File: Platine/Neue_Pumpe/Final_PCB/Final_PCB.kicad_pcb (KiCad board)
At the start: 2 copper layers, 27.5 x 27.5 mm, 1 part

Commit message: a lot of advance in final PCB
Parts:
- added C1: 100p, Capacitor_SMD:C_0603_1608Metric_Pad1.08x0.95mm_HandSolder, F.Cu at (50.1, -51.1)
- added C10: 100p, Capacitor_SMD:C_0603_1608Metric_Pad1.08x0.95mm_HandSolder, F.Cu at (50.1, -28.5)
- added C11: 100p, Capacitor_SMD:C_0603_1608Metric_Pad1.08x0.95mm_HandSolder, F.Cu at (50.1, -26.0)
- added C12: 100p, Capacitor_SMD:C_0603_1608Metric_Pad1.08x0.95mm_HandSolder, F.Cu at (50.1, -23.5)
- added C13: 100p, Capacitor_SMD:C_0603_1608Metric_Pad1.08x0.95mm_HandSolder, F.Cu at (50.1, -21.0)
- added C14: 100p, Capacitor_SMD:C_0603_1608Metric_Pad1.08x0.95mm_HandSolder, F.Cu at (54.5, -51.1)
- added C15: 100p, Capacitor_SMD:C_0603_1608Metric_Pad1.08x0.95mm_HandSolder, F.Cu at (54.5, -48.6)
- added C16: 100p, Capacitor_SMD:C_0603_1608Metric_Pad1.08x0.95mm_HandSolder, F.Cu at (54.5, -46.1)
- added C17: 100p, Capacitor_SMD:C_0603_1608Metric_Pad1.08x0.95mm_HandSolder, F.Cu at (54.5, -43.6)
- added C18: 100p, Capacitor_SMD:C_0603_1608Metric_Pad1.08x0.95mm_HandSolder, F.Cu at (54.5, -41.1)
- added C19: 100n, Capacitor_SMD:C_0603_1608Metric_Pad1.08x0.95mm_HandSolder, F.Cu at (54.5, -38.6)
- added C2: 100p, Capacitor_SMD:C_0603_1608Metric_Pad1.08x0.95mm_HandSolder, F.Cu at (50.1, -48.6)
- added C20: 100n, Capacitor_SMD:C_0603_1608Metric_Pad1.08x0.95mm_HandSolder, F.Cu at (54.5, -36.1)
- added C21: 100n, Capacitor_SMD:C_0603_1608Metric_Pad1.08x0.95mm_HandSolder, F.Cu at (54.5, -33.5)
- added C22: 10u, Capacitor_SMD:C_0603_1608Metric_Pad1.08x0.95mm_HandSolder, F.Cu at (78.2, 6.53)
- added C23: 10u, Capacitor_SMD:C_0603_1608Metric_Pad1.08x0.95mm_HandSolder, F.Cu at (78.2, 9.04)
- added C24: 0.1uF, Capacitor_SMD:C_0603_1608Metric_Pad1.08x0.95mm_HandSolder, F.Cu at (79.1, 37.1)
- added C25: 0.1uF, Capacitor_SMD:C_0603_1608Metric_Pad1.08x0.95mm_HandSolder, F.Cu at (79.3, 28.1)
- added C26: 0.1uF, Capacitor_SMD:C_0603_1608Metric_Pad1.08x0.95mm_HandSolder, F.Cu at (93.5, 41.6)
- added C27: 0.1uF, Capacitor_SMD:C_0603_1608Metric_Pad1.08x0.95mm_HandSolder, F.Cu at (86.3, 37.5)
- added C28: 0.1uF, Capacitor_SMD:C_0603_1608Metric_Pad1.08x0.95mm_HandSolder, F.Cu at (72.4, 37.1)
- added C29: 0.1uF, Capacitor_SMD:C_0603_1608Metric_Pad1.08x0.95mm_HandSolder, F.Cu at (72.3, 28.1)
- added C3: 100p, Capacitor_SMD:C_0603_1608Metric_Pad1.08x0.95mm_HandSolder, F.Cu at (50.1, -46.1)
- added C30: 0.1uF, Capacitor_SMD:C_0603_1608Metric_Pad1.08x0.95mm_HandSolder, B.Cu at (80.3, 43.1)
- added C31: 0.1uF, Capacitor_SMD:C_0603_1608Metric_Pad1.08x0.95mm_HandSolder, F.Cu at (65.8, 37.1)
- added C32: 0.1uF, Capacitor_SMD:C_0603_1608Metric_Pad1.08x0.95mm_HandSolder, B.Cu at (78.3, 35.7)
- added C33: 0.1uF, Capacitor_SMD:C_0603_1608Metric_Pad1.08x0.95mm_HandSolder, F.Cu at (82.6, -26.4)
- added C34: 0.1uF, Capacitor_SMD:C_0603_1608Metric_Pad1.08x0.95mm_HandSolder, F.Cu at (82.6, -23.9)
- added C35: 0.1uF, Capacitor_SMD:C_0603_1608Metric_Pad1.08x0.95mm_HandSolder, F.Cu at (82.6, -21.3)
- added C36: 0.1uF, Capacitor_SMD:C_0603_1608Metric_Pad1.08x0.95mm_HandSolder, F.Cu at (82.6, -18.8)
- added C37: 0.1uF, Capacitor_SMD:C_0603_1608Metric_Pad1.08x0.95mm_HandSolder, F.Cu at (66.6, 28.1)
- added C38: 0.1uF, Capacitor_SMD:C_0603_1608Metric_Pad1.08x0.95mm_HandSolder, F.Cu at (86.9, -31.4)
- added C39: 0.1uF, Capacitor_SMD:C_0603_1608Metric_Pad1.08x0.95mm_HandSolder, F.Cu at (86.9, -28.9)
- added C4: 100p, Capacitor_SMD:C_0603_1608Metric_Pad1.08x0.95mm_HandSolder, F.Cu at (50.1, -43.6)
- added C40: 0.1uF, Capacitor_SMD:C_0603_1608Metric_Pad1.08x0.95mm_HandSolder, F.Cu at (86.9, -26.4)
- added C41: 0.1uF, Capacitor_SMD:C_0603_1608Metric_Pad1.08x0.95mm_HandSolder, F.Cu at (86.9, -23.9)
- added C5: 100p, Capacitor_SMD:C_0603_1608Metric_Pad1.08x0.95mm_HandSolder, F.Cu at (50.1, -41.1)
- added C6: 100p, Capacitor_SMD:C_0603_1608Metric_Pad1.08x0.95mm_HandSolder, F.Cu at (50.1, -38.6)
- added C7: 100p, Capacitor_SMD:C_0603_1608Metric_Pad1.08x0.95mm_HandSolder, F.Cu at (50.1, -36.1)
- added C8: 100p, Capacitor_SMD:C_0603_1608Metric_Pad1.08x0.95mm_HandSolder, F.Cu at (50.1, -33.5)
- added C9: 100p, Capacitor_SMD:C_0603_1608Metric_Pad1.08x0.95mm_HandSolder, F.Cu at (50.1, -31.0)
- added J3: Conn_01x10, FLE-105-01-G-DV-K-TR:FLE-105-01-X-DV-Y-TR, B.Cu at (38.8, 38.0)
- added J4: Conn_01x10, Samtec-FTSH-105-01-L-DV-K:FTSH-105-01-L-DV-K, F.Cu at (72.4, 41.7)
- added J5: Conn_01x10, FLE-105-01-G-DV-K-TR:FLE-105-01-X-DV-Y-TR, B.Cu at (39.3, 72.5)
- added J6: Conn_01x06, Connector_PinHeader_1.27mm:PinHeader_2x03_P1.27mm_Vertical_SMD, B.Cu at (77.8, 46.3)
- added J7: Conn_01x06, Connector_PinHeader_1.27mm:PinHeader_2x03_P1.27mm_Vertical_SMD, B.Cu at (73.1, 41.4)
- added R1: 1k, Resistor_SMD:R_0603_1608Metric_Pad0.98x0.95mm_HandSolder, F.Cu at (54.5, -31.0)
- added R10: 1k, Resistor_SMD:R_0603_1608Metric_Pad0.98x0.95mm_HandSolder, F.Cu at (58.8, -41.1)
- added R11: 100k, Resistor_SMD:R_0603_1608Metric_Pad0.98x0.95mm_HandSolder, F.Cu at (58.8, -38.6)
- added R12: 100k, Resistor_SMD:R_0603_1608Metric_Pad0.98x0.95mm_HandSolder, F.Cu at (58.8, -36.1)
- added R13: 100k, Resistor_SMD:R_0603_1608Metric_Pad0.98x0.95mm_HandSolder, F.Cu at (58.8, -33.5)
- added R14: 100k, Resistor_SMD:R_0603_1608Metric_Pad0.98x0.95mm_HandSolder, F.Cu at (58.8, -31.0)
- added R15: 252k, Resistor_SMD:R_0603_1608Metric_Pad0.98x0.95mm_HandSolder, F.Cu at (58.8, -28.5)
- added R16: 252k, Resistor_SMD:R_0603_1608Metric_Pad0.98x0.95mm_HandSolder, F.Cu at (58.8, -26.0)
- added R17: 252k, Resistor_SMD:R_0603_1608Metric_Pad0.98x0.95mm_HandSolder, F.Cu at (58.8, -23.5)
- added R18: 252k, Resistor_SMD:R_0603_1608Metric_Pad0.98x0.95mm_HandSolder, F.Cu at (58.8, -21.0)
- added R19: 1k, Resistor_SMD:R_0603_1608Metric_Pad0.98x0.95mm_HandSolder, F.Cu at (63.2, -51.1)
- added R2: 1k, Resistor_SMD:R_0603_1608Metric_Pad0.98x0.95mm_HandSolder, F.Cu at (54.5, -28.5)
- added R20: 1k, Resistor_SMD:R_0603_1608Metric_Pad0.98x0.95mm_HandSolder, F.Cu at (63.2, -48.6)
- added R21: 1k, Resistor_SMD:R_0603_1608Metric_Pad0.98x0.95mm_HandSolder, F.Cu at (63.2, -46.1)
- added R22: 1k, Resistor_SMD:R_0603_1608Metric_Pad0.98x0.95mm_HandSolder, F.Cu at (63.2, -43.6)
- added R23: 1k, Resistor_SMD:R_0603_1608Metric_Pad0.98x0.95mm_HandSolder, F.Cu at (63.2, -41.1)
- added R24: 1k, Resistor_SMD:R_0603_1608Metric_Pad0.98x0.95mm_HandSolder, F.Cu at (63.2, -38.6)
- added R25: 100k, Resistor_SMD:R_0603_1608Metric_Pad0.98x0.95mm_HandSolder, F.Cu at (63.2, -36.1)
- added R26: 100k, Resistor_SMD:R_0603_1608Metric_Pad0.98x0.95mm_HandSolder, F.Cu at (63.2, -33.5)
- added R27: 100k, Resistor_SMD:R_0603_1608Metric_Pad0.98x0.95mm_HandSolder, F.Cu at (63.2, -31.0)
- added R28: 100k, Resistor_SMD:R_0603_1608Metric_Pad0.98x0.95mm_HandSolder, F.Cu at (63.2, -28.5)
- added R29: 100k, Resistor_SMD:R_0603_1608Metric_Pad0.98x0.95mm_HandSolder, F.Cu at (63.2, -26.0)
- added R3: 100k, Resistor_SMD:R_0603_1608Metric_Pad0.98x0.95mm_HandSolder, F.Cu at (54.5, -26.0)
- added R30: 100k, Resistor_SMD:R_0603_1608Metric_Pad0.98x0.95mm_HandSolder, F.Cu at (63.2, -23.5)
- added R31: 252k, Resistor_SMD:R_0603_1608Metric_Pad0.98x0.95mm_HandSolder, F.Cu at (63.2, -21.0)
- added R32: 252k, Resistor_SMD:R_0603_1608Metric_Pad0.98x0.95mm_HandSolder, F.Cu at (67.5, -51.1)
- added R33: 252k, Resistor_SMD:R_0603_1608Metric_Pad0.98x0.95mm_HandSolder, F.Cu at (67.5, -48.6)
- added R34: 252k, Resistor_SMD:R_0603_1608Metric_Pad0.98x0.95mm_HandSolder, F.Cu at (67.5, -46.1)
- added R35: 252k, Resistor_SMD:R_0603_1608Metric_Pad0.98x0.95mm_HandSolder, F.Cu at (67.5, -43.6)
- added R36: 252k, Resistor_SMD:R_0603_1608Metric_Pad0.98x0.95mm_HandSolder, F.Cu at (67.5, -41.1)
- added R37: 1k, Resistor_SMD:R_0603_1608Metric_Pad0.98x0.95mm_HandSolder, F.Cu at (67.5, -38.6)
- added R38: 1k, Resistor_SMD:R_0603_1608Metric_Pad0.98x0.95mm_HandSolder, F.Cu at (67.5, -36.1)
- added R39: 1k, Resistor_SMD:R_0603_1608Metric_Pad0.98x0.95mm_HandSolder, F.Cu at (67.5, -33.5)
- added R4: 100k, Resistor_SMD:R_0603_1608Metric_Pad0.98x0.95mm_HandSolder, F.Cu at (54.5, -23.5)
- added R40: 1k, Resistor_SMD:R_0603_1608Metric_Pad0.98x0.95mm_HandSolder, F.Cu at (67.5, -31.0)
- added R41: 1k, Resistor_SMD:R_0603_1608Metric_Pad0.98x0.95mm_HandSolder, F.Cu at (67.5, -28.5)
- added R42: 1k, Resistor_SMD:R_0603_1608Metric_Pad0.98x0.95mm_HandSolder, F.Cu at (67.5, -26.0)
- added R43: 100k, Resistor_SMD:R_0603_1608Metric_Pad0.98x0.95mm_HandSolder, F.Cu at (67.5, -23.5)
- added R44: 100k, Resistor_SMD:R_0603_1608Metric_Pad0.98x0.95mm_HandSolder, F.Cu at (67.5, -21.0)
- added R45: 100k, Resistor_SMD:R_0603_1608Metric_Pad0.98x0.95mm_HandSolder, F.Cu at (71.9, -51.1)
- added R46: 100k, Resistor_SMD:R_0603_1608Metric_Pad0.98x0.95mm_HandSolder, F.Cu at (71.9, -48.6)
- added R47: 100k, Resistor_SMD:R_0603_1608Metric_Pad0.98x0.95mm_HandSolder, F.Cu at (71.9, -46.1)
- added R48: 100k, Resistor_SMD:R_0603_1608Metric_Pad0.98x0.95mm_HandSolder, F.Cu at (71.9, -43.6)
- added R49: 252k, Resistor_SMD:R_0603_1608Metric_Pad0.98x0.95mm_HandSolder, F.Cu at (71.9, -41.1)
- added R5: 252k, Resistor_SMD:R_0603_1608Metric_Pad0.98x0.95mm_HandSolder, F.Cu at (54.5, -21.0)
- added R50: 252k, Resistor_SMD:R_0603_1608Metric_Pad0.98x0.95mm_HandSolder, F.Cu at (71.9, -38.6)
- added R51: 252k, Resistor_SMD:R_0603_1608Metric_Pad0.98x0.95mm_HandSolder, F.Cu at (71.9, -36.1)
- added R52: 252k, Resistor_SMD:R_0603_1608Metric_Pad0.98x0.95mm_HandSolder, F.Cu at (71.9, -33.5)
- added R53: 252k, Resistor_SMD:R_0603_1608Metric_Pad0.98x0.95mm_HandSolder, F.Cu at (71.9, -31.0)
- added R54: 252k, Resistor_SMD:R_0603_1608Metric_Pad0.98x0.95mm_HandSolder, F.Cu at (71.9, -28.5)
- added R55: 12.5, Resistor_SMD:R_0603_1608Metric_Pad0.98x0.95mm_HandSolder, F.Cu at (82.5, 37.1)
- added R56: 12.5, Resistor_SMD:R_0603_1608Metric_Pad0.98x0.95mm_HandSolder, F.Cu at (77.7, 42.4)
- added R57: 12.5, Resistor_SMD:R_0603_1608Metric_Pad0.98x0.95mm_HandSolder, F.Cu at (75.8, 37.1)
- added R58: 12.5, Resistor_SMD:R_0603_1608Metric_Pad0.98x0.95mm_HandSolder, B.Cu at (79.4, 39.3)
- added R59: 12.5, Resistor_SMD:R_0603_1608Metric_Pad0.98x0.95mm_HandSolder, F.Cu at (69.1, 37.1)
- added R6: 252k, Resistor_SMD:R_0603_1608Metric_Pad0.98x0.95mm_HandSolder, F.Cu at (58.8, -51.1)
- added R60: 12.5, Resistor_SMD:R_0603_1608Metric_Pad0.98x0.95mm_HandSolder, B.Cu at (74.8, 35.8)
- added R61: 12.5, Resistor_SMD:R_0603_1608Metric_Pad0.98x0.95mm_HandSolder, B.Cu at (81.7, 35.8)
- added R62: 12.5, Resistor_SMD:R_0603_1608Metric_Pad0.98x0.95mm_HandSolder, B.Cu at (63.3, 55.2)
- added R63: 12.5, Resistor_SMD:R_0603_1608Metric_Pad0.98x0.95mm_HandSolder, B.Cu at (67.3, 35.8)
- added R7: 1k, Resistor_SMD:R_0603_1608Metric_Pad0.98x0.95mm_HandSolder, F.Cu at (58.8, -48.6)
- added R8: 1k, Resistor_SMD:R_0603_1608Metric_Pad0.98x0.95mm_HandSolder, F.Cu at (58.8, -46.1)
- added R9: 1k, Resistor_SMD:R_0603_1608Metric_Pad0.98x0.95mm_HandSolder, F.Cu at (58.8, -43.6)
- added REF**: MountingHole_3mm, MountingHole:MountingHole_3mm, F.Cu at (75.5, 24.5)
- added REF**: MountingHole_3mm, MountingHole:MountingHole_3mm, F.Cu at (39.2, 59.6)
- added U1: ~, Package_SO:SOIC-14_3.9x8.7mm_P1.27mm, F.Cu at (52.2, -14.5)
- added U10: ~, Package_SO:SOP-8_3.9x4.9mm_P1.27mm, B.Cu at (75.1, 31.3)
- added U11: ~, Package_SO:SOP-8_3.9x4.9mm_P1.27mm, B.Cu at (82.7, 31.3)
- added U12: ~, Package_SO:SOP-8_3.9x4.9mm_P1.27mm, B.Cu at (58.8, 54.9)
- added U13: ~, Package_SO:SOP-8_3.9x4.9mm_P1.27mm, B.Cu at (67.6, 31.3)
- added U2: ~, Package_SO:SOIC-14_3.9x8.7mm_P1.27mm, F.Cu at (60.6, -14.5)
- added U3: ~, Package_SO:SOIC-14_3.9x8.7mm_P1.27mm, F.Cu at (69.1, -14.5)
- added U4: ~, Package_DIP:SMDIP-8_W9.53mm, F.Cu at (92.4, -7.19)
- added U5: ~, Package_SO:SOP-8_3.9x4.9mm_P1.27mm, F.Cu at (82.2, 32.6)
- added U6: ~, Package_SO:SOP-8_3.9x4.9mm_P1.27mm, F.Cu at (82.3, 42.1)
- added U7: ~, Package_SO:SOP-8_3.9x4.9mm_P1.27mm, F.Cu at (75.3, 32.6)
- added U8: ~, Package_SO:SOP-8_3.9x4.9mm_P1.27mm, B.Cu at (83.9, 39.6)
- added U9: ~, Package_SO:SOP-8_3.9x4.9mm_P1.27mm, F.Cu at (68.5, 32.6)
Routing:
- net /analog_inp_9: track 0.00 -> 15.2 mm, vias 0 -> 2
- net /analog_inp_8: track 0.00 -> 15.2 mm, vias 0 -> 2
- net /analog_inp_7: track 0.00 -> 15.0 mm, vias 0 -> 2
- net /analog_inp_4: track 0.00 -> 13.3 mm, vias 0 -> 2
- net /analog_inp_6: track 0.00 -> 11.1 mm, vias 0 -> 2
- net /analog_inp_5: track 0.00 -> 9.82 mm, vias 0 -> 2
- net /analog_inp_2: track 0.00 -> 8.37 mm, vias 0 -> 2
- net /analog_inp_1: track 0.00 -> 6.81 mm, vias 0 -> 2
- net /analog_inp_3: track 0.00 -> 5.89 mm, vias 0 -> 2
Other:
- board size 27.5 x 27.5 mm -> 64.4 x 62.7 mm
- board text added: "Plate type 1"
- board text added: "Plate type 2"

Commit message: still need to finish routing
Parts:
- added C42: 10n, Capacitor_SMD:C_0603_1608Metric_Pad1.08x0.95mm_HandSolder, F.Cu at (87.2, 32.3)
- added C43: 10n, Capacitor_SMD:C_0603_1608Metric_Pad1.08x0.95mm_HandSolder, F.Cu at (79.8, 47.7)
- added C44: 10n, Capacitor_SMD:C_0603_1608Metric_Pad1.08x0.95mm_HandSolder, B.Cu at (71.8, 26.6)
- added C45: 10n, Capacitor_SMD:C_0603_1608Metric_Pad1.08x0.95mm_HandSolder, F.Cu at (87.2, 80.0)
- added C46: 10n, Capacitor_SMD:C_0603_1608Metric_Pad1.08x0.95mm_HandSolder, F.Cu at (68.9, 26.6)
- added C47: 10n, Capacitor_SMD:C_0603_1608Metric_Pad1.08x0.95mm_HandSolder, B.Cu at (87.1, 37.7)
- added C48: 10n, Capacitor_SMD:C_0603_1608Metric_Pad1.08x0.95mm_HandSolder, B.Cu at (76.4, 48.1)
- added C49: 10n, Capacitor_SMD:C_0603_1608Metric_Pad1.08x0.95mm_HandSolder, F.Cu at (87.3, 74.6)
- added C50: 10n, Capacitor_SMD:C_0603_1608Metric_Pad1.08x0.95mm_HandSolder, B.Cu at (87.3, 33.3)
- added J1: Conn_01x12, SHF-106-01-L-D-SM:SHF-106-01-L-D-SM, F.Cu at (81.4, 90.3)
- added J8: Conn_01x08, Connector_PinHeader_1.27mm:PinHeader_2x04_P1.27mm_Horizontal, B.Cu at (72.7, 64.3)
- added J9: Conn_01x06, Connector_PinHeader_1.27mm:PinHeader_2x03_P1.27mm_Horizontal, F.Cu at (64.0, 64.3)
- added R64: 1k, Resistor_SMD:R_0603_1608Metric_Pad0.98x0.95mm_HandSolder, F.Cu at (85.7, 32.3)
- added R65: 1k, Resistor_SMD:R_0603_1608Metric_Pad0.98x0.95mm_HandSolder, F.Cu at (79.8, 46.2)
- added R66: 1k, Resistor_SMD:R_0603_1608Metric_Pad0.98x0.95mm_HandSolder, B.Cu at (71.8, 28.1)
- added R67: 1k, Resistor_SMD:R_0603_1608Metric_Pad0.98x0.95mm_HandSolder, F.Cu at (85.8, 80.0)
- added R68: 1k, Resistor_SMD:R_0603_1608Metric_Pad0.98x0.95mm_HandSolder, F.Cu at (68.9, 28.1)
- added R69: 1k, Resistor_SMD:R_0603_1608Metric_Pad0.98x0.95mm_HandSolder, B.Cu at (86.2, 40.1)
- added R70: 1k, Resistor_SMD:R_0603_1608Metric_Pad0.98x0.95mm_HandSolder, B.Cu at (73.1, 48.1)
- added R71: 1k, Resistor_SMD:R_0603_1608Metric_Pad0.98x0.95mm_HandSolder, F.Cu at (85.8, 74.6)
- added R72: 1k, Resistor_SMD:R_0603_1608Metric_Pad0.98x0.95mm_HandSolder, B.Cu at (85.8, 31.5)
- C10, C11, C12, C13, C14, C15, C16, C17, C18, C20, C21, C23, C33, C35, C38, C39, C41, C7, C8, C9, R19, R20, R21, R22, R23, R24, R25, R26, R27, R28, R29, R30, R31, R32, R33, R34, R35, R36, R37, R38, R39, R40, R41, R42, R43, R44, R45, R46, R47, R48, R49, R50, R51, R52, R53, R54, U2, U3: moved to B.Cu
- C30, R58, R62, U12, U8: moved to F.Cu
- J6: value Conn_01x06 -> Conn_01x08; footprint Connector_PinHeader_1.27mm:PinHeader_2x03_P1.27mm_Vertical_SMD -> Connector_PinHeader_1.27mm_modified:PinHeader_2x04_P1.27mm_Vertical_SMD
- moved R19 142.7 mm to (87.3, 89.5)
- moved R20 141.8 mm to (87.3, 91.2), turned to 180 degrees
- moved R7 139.6 mm to (72.2, 90.4)
- moved C1 139.2 mm to (66.2, 87.2), turned to 90 degrees
- moved C14 139.2 mm to (66.4, 87.6), turned to 90 degrees
- moved R8 138.7 mm to (72.2, 92.0), turned to 180 degrees
- moved R32 136.1 mm to (78.2, 84.6), turned to -90 degrees
- moved C3 134.9 mm to (71.3, 87.1), turned to 90 degrees
- moved R21 134.8 mm to (79.0, 87.8), turned to 180 degrees
- moved R6 134.1 mm to (65.2, 82.8), turned to 180 degrees
- moved R22 134.0 mm to (79.0, 89.5)
- moved R46 133.6 mm to (72.5, 85.0)
- moved R47 131.2 mm to (65.5, 85.0), turned to 180 degrees
- moved C2 130.6 mm to (65.2, 81.2)
- moved R37 129.6 mm to (70.7, 91.0)
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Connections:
- J6 pad 1: unconnected-(J6-Pin_1-Pad1) -> /fil_da5
- J6 pad 2: unconnected-(J6-Pin_2-Pad2) -> /analog_inp_8
- J6 pad 3: unconnected-(J6-Pin_3-Pad3) -> /fil_da3
- J6 pad 4: unconnected-(J6-Pin_4-Pad4) -> /analog_inp_4
- J6 pad 5: unconnected-(J6-Pin_5-Pad5) -> /fil_da1
- J6 pad 6: unconnected-(J6-Pin_6-Pad6) -> +3.3VA
- J7 pad 1: unconnected-(J7-Pin_1-Pad1) -> GNDD
- J7 pad 2: unconnected-(J7-Pin_2-Pad2) -> +3.3VD
- J7 pad 3: unconnected-(J7-Pin_3-Pad3) -> /fil_da2
- J7 pad 4: unconnected-(J7-Pin_4-Pad4) -> /fil_da7
- J7 pad 6: unconnected-(J7-Pin_6-Pad6) -> /fil_da6
- R13 pad 2: /Signal conditioning/data_in2 -> /fil_da2
- R14 pad 2: /Signal conditioning/data_in3 -> /fil_da3
- R28 pad 2: /Signal conditioning/data_in4 -> /fil_da4
- R29 pad 2: /Signal conditioning/data_in5 -> /fil_da5
- R30 pad 2: /Signal conditioning/data_in6 -> /fil_da6
- R4 pad 2: /Signal conditioning/data_in1 -> /fil_da1
- R46 pad 2: /Signal conditioning/data_in7 -> /fil_da7
- R47 pad 2: /Signal conditioning/data_in8 -> /fil_da8
- R48 pad 2: /Signal conditioning/data_in9 -> /fil_da9
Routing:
- net +3.3VA: track 0.00 -> 35.9 mm, vias 0 -> 4
- net /fil_da2: track 0.00 -> 30.2 mm, vias 0 -> 1
- net /fil_da6: track 0.00 -> 27.6 mm
- net /fil_da1: track 0.00 -> 21.0 mm, vias 0 -> 1
- net /fil_da9: track 0.00 -> 20.7 mm
- net /analog_inp_3: track 5.89 -> 22.6 mm
- net /fil_da7: track 0.00 -> 16.2 mm
- net /analog_inp_9: track 15.2 -> 30.0 mm, vias 2 -> 3
- net /analog_inp_4: track 13.3 -> 26.5 mm, vias 2 -> 3
- net /analog_inp_8: track 15.2 -> 28.1 mm, vias 2 -> 3
- net +3.3VD: track 0.00 -> 11.8 mm
- net /analog_inp_2: track 8.37 -> 19.7 mm
- net /analog_inp_6: track 11.1 -> 20.9 mm, vias 2 -> 3
- net /analog_inp_1: track 6.81 -> 15.8 mm
- net /fil_da5: track 0.00 -> 7.17 mm, vias 0 -> 1
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- added copper zone on B.Cu, net GNDA
- added copper zone on F.Cu, net GNDA
- added copper zone on B.Cu, net GNDD
- added copper zone on F.Cu, net GNDD
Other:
- board size 64.4 x 62.7 mm -> 64.5 x 73.1 mm
- board text added: "** Grid: The tip of the cupper is to be sold to a mini banana connector ** The circle cut must be adapted to the screw-connector width, a cable will be solded behind, which goes to another mini-banana connector that connects finally to the assembly"
- board text added: "2mm connector plastic, female"

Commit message: Almost done with routing
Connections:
- J1 pad 11: /VPlatte(GNDA) -> GNDA
- J7 pad 5: unconnected-(J7-Pin_5-Pad5) -> /fil_da1
- J8 pad 1: /fil_da5 -> /fil_da9
- J8 pad 2: /analog_inp_8 -> GNDA
- J8 pad 3: /fil_da3 -> unconnected-(J8-Pin_3-Pad3)
- J8 pad 4: /analog_inp_4 -> +3.3VA
- J8 pad 5: /fil_da1 -> /fil_da3
- J8 pad 6: +3.3VA -> /analog_inp_4
- J8 pad 7: /fil_da9 -> /fil_da5
- J8 pad 8: GNDA -> /analog_inp_8
- J9 pad 5: unconnected-(J9-Pin_5-Pad5) -> /fil_da1
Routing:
- net /Out9: track 0.00 -> 52.1 mm, vias 0 -> 3
- net /fil_da8: track 0.00 -> 51.5 mm, vias 0 -> 1
- net +3.3VA: track 35.9 -> 80.8 mm, vias 4 -> 6
- net GNDA: track 2.10 -> 46.4 mm, vias 0 -> 3
- net /fil_da7: track 16.2 -> 54.6 mm, vias 0 -> 2
- net /Out8: track 0.00 -> 36.0 mm, vias 0 -> 1
- net /Out1: track 0.00 -> 35.4 mm, vias 0 -> 4
- net +3.3VD: track 11.8 -> 47.0 mm
- net /fil_da1: track 21.0 -> 53.4 mm
- net /fil_da2: track 30.2 -> 61.0 mm, vias 1 -> 2
- net /analog_inp_4: track 26.5 -> 55.3 mm, vias 3 -> 5
- net /Out6: track 0.00 -> 25.1 mm, vias 0 -> 3
- net /Out3: track 0.00 -> 24.2 mm, vias 0 -> 2
- net /fil_da5: track 7.17 -> 30.9 mm, vias 1 -> 2
- net /fil_da9: track 20.7 -> 43.5 mm, vias 0 -> 3
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
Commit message: final PCB finished
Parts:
- removed C19: 100n, Capacitor_SMD:C_0603_1608Metric_Pad1.08x0.95mm_HandSolder
- removed C26, C33: 0.1uF, Capacitor_SMD:C_0603_1608Metric_Pad1.08x0.95mm_HandSolder
- added J2: Conn_01x10, FLE-105-01-G-DV-K-TR:FLE-105-01-X-DV-Y-TR, B.Cu at (34.5, 111.5)
- added REF**: MountingHole_3mm, MountingHole:MountingHole_3mm, F.Cu at (38.0, 92.3)
- moved C47 9.19 mm to (82.5, 45.6), turned to 180 degrees
- moved R10 1.88 mm to (66.2, 71.2), turned to -90 degrees
- moved C44 1.68 mm to (70.2, 26.5), turned to 180 degrees
- moved R63 1.27 mm to (76.0, 31.5), turned to 0 degrees
- moved R9 0.27 mm to (64.2, 68.8)
- moved C25 0.27 mm to (81.8, 27.9)
- moved R60 0.23 mm to (77.0, 39.2)
- turned R69 to -90 degrees
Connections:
- J7 pad 1: GNDD -> /fil_da1
- J7 pad 5: /fil_da1 -> GNDD
- J9 pad 1: GNDD -> /fil_da1
- J9 pad 5: /fil_da1 -> GNDD
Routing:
- net +3.3VD: track 47.0 -> 196.9 mm, vias 0 -> 15
- net GNDA: track 46.4 -> 75.6 mm, vias 3 -> 14
- net GNDD: track 0.00 -> 7.19 mm, vias 0 -> 32
- net /analog_inp_5: track 16.9 -> 20.6 mm, vias 2 -> 3
- net /analog_inp_3: track 22.6 -> 25.9 mm, vias 2 -> 3
- net /analog_inp_7: track 18.9 -> 21.9 mm, vias 3 -> 4
- net /analog_inp_8: track 47.7 -> 50.3 mm, vias 3 -> 4
- net /analog_inp_6: track 20.9 -> 23.0 mm, vias 3 -> 4
- net +3.3VA: track 80.8 -> 82.8 mm
- net /analog_inp_1: track 15.8 -> 17.7 mm, vias 2 -> 3
- net /analog_inp_4: track 55.3 -> 57.2 mm, vias 5 -> 6
- net /fil_da9: track 43.5 -> 45.2 mm
- net /fil_da2: track 61.0 -> 59.4 mm
- net /analog_inp_2: track 19.7 -> 21.2 mm, vias 2 -> 3
- net /fil_da6: track 40.4 -> 39.6 mm
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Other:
- board size 64.5 x 73.1 mm -> 65.1 x 95.3 mm
- board text added: "GNDA Out4 3V3D GD Out9 Out8"
- board text added: "Out5 Out6 Out3 Out2 Out7 Out1"
- board text added: "Plate type 2.1"
- board text added: "Plate type 2.2"
- board text removed: "Plate type 2"

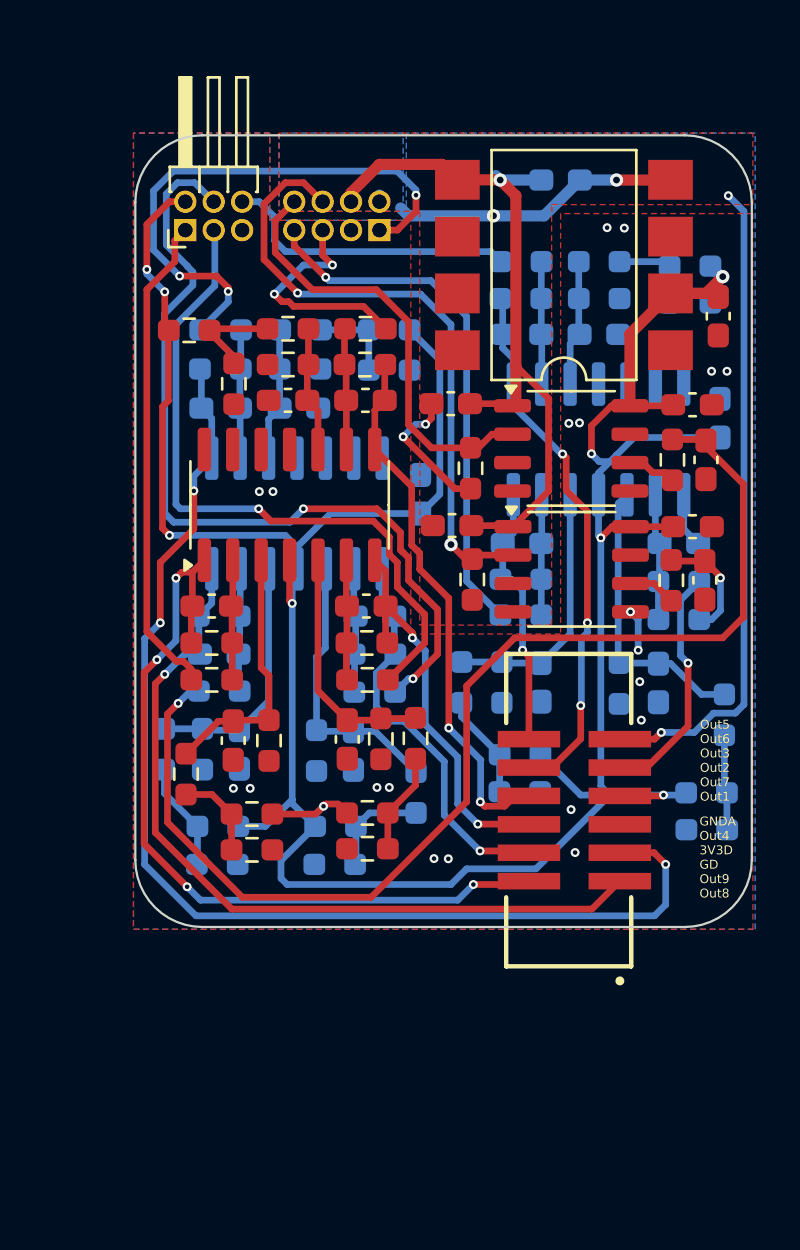
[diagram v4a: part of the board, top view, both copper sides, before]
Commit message: Added grid voltage connector
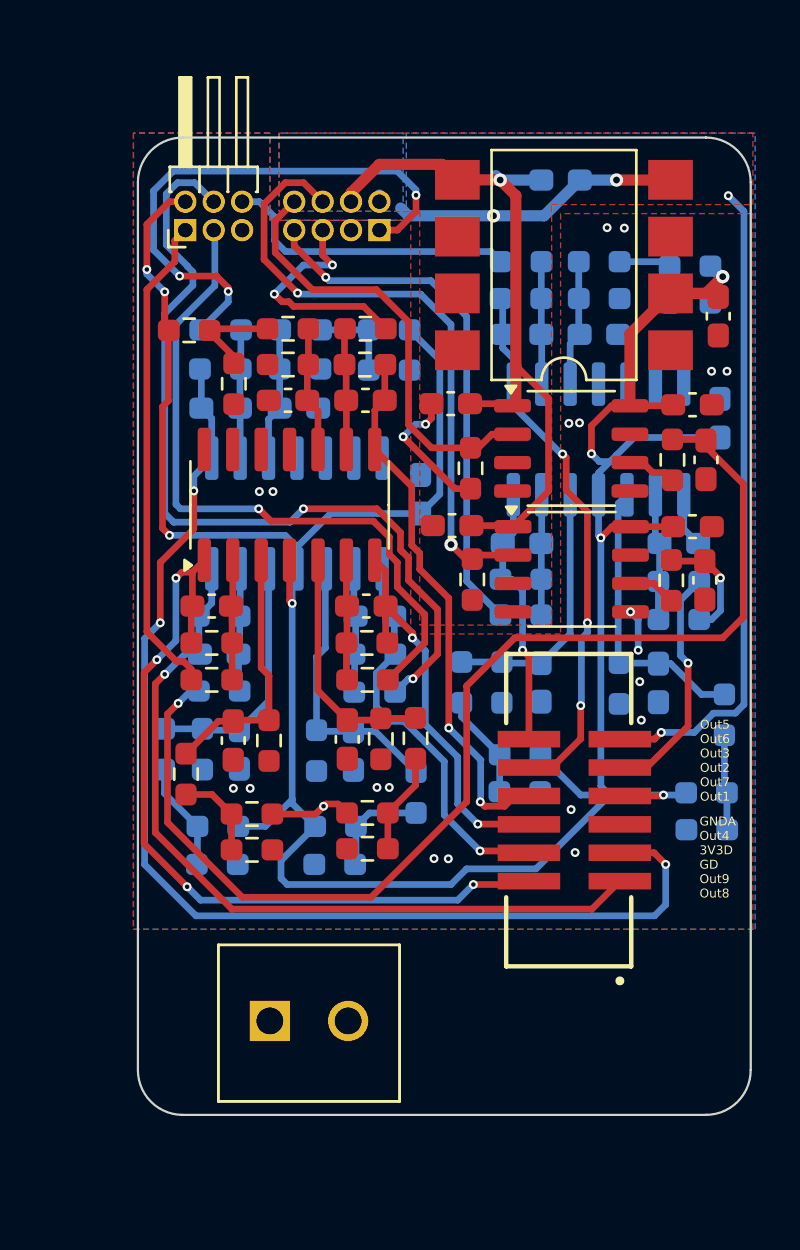
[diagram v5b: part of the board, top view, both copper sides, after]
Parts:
- added J10: Conn_01x02, OSTTE020104:OST_OSTTE020104, F.Cu at (69.5, 99.7)
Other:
- outline, holes or cut-outs redrawn
- board text added: "High voltage connector (>1 kV)"
- board text added: "Sensor PCB"
- board text added: "Sig. Cond. PCB"
